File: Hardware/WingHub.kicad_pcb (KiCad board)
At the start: 2 copper layers, 50.8 x 22.9 mm, 17 parts, among them J1 feather long, J2 feather short, J3 USB_A, SW1 RESET, SW2 DOWNLOADER, U1 CH559T

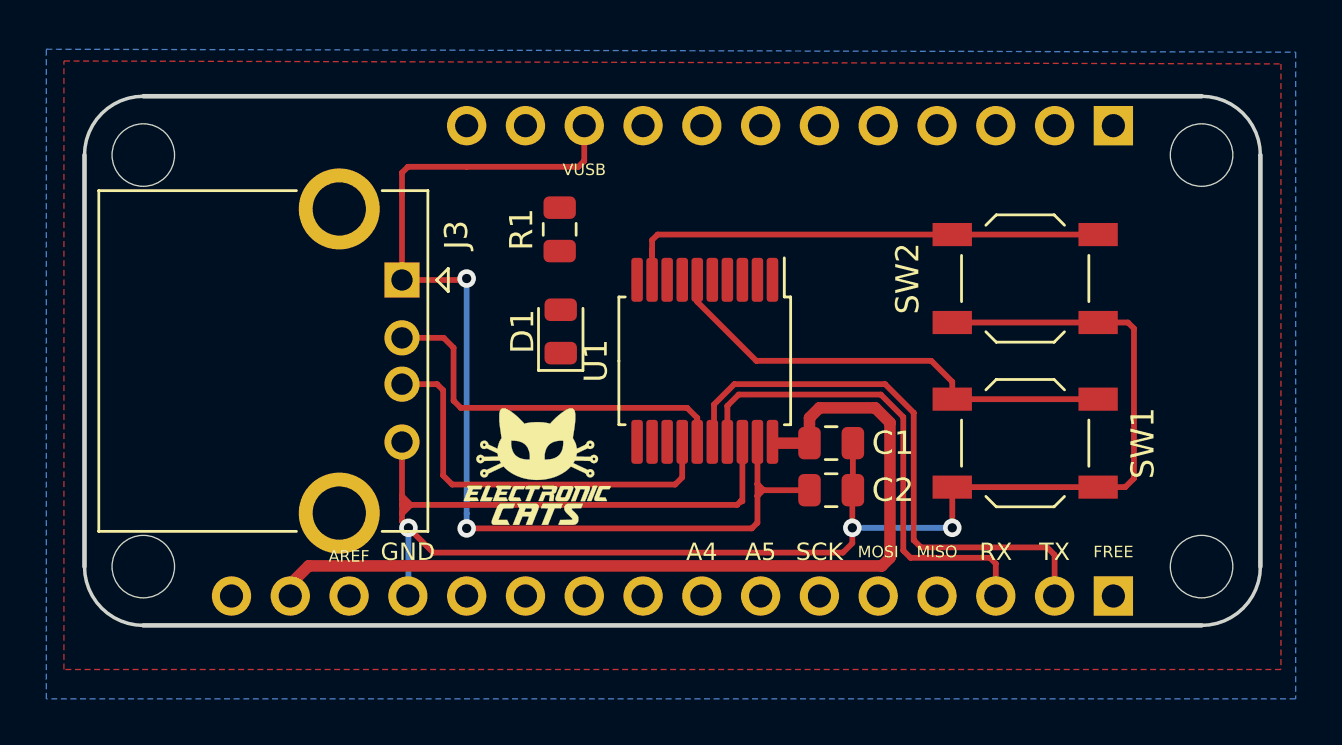
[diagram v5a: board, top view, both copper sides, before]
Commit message: Added electronic devices are routed.
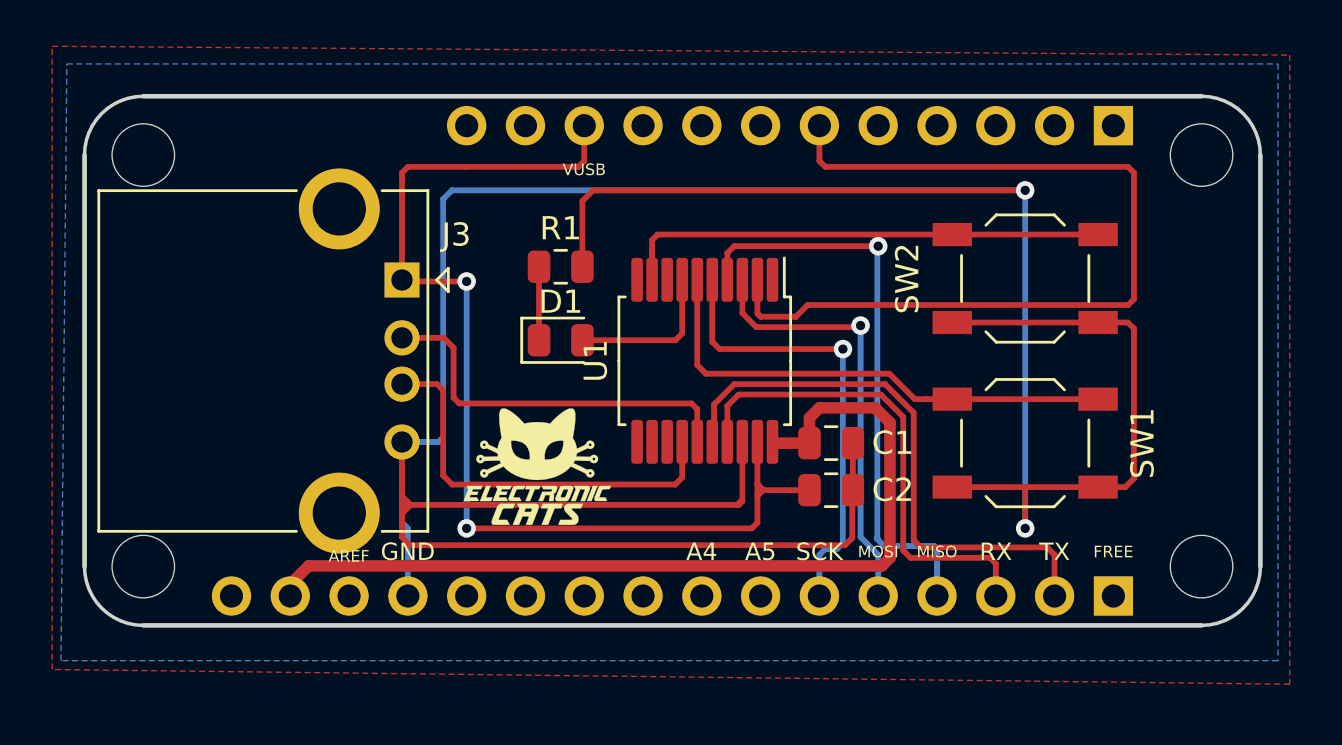
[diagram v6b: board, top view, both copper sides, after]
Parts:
- moved R1 1.62 mm to (46.0, 32.8), turned to 0 degrees
- moved D1 0.38 mm to (46.0, 35.9), turned to 0 degrees
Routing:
- net GND: track 79.2 -> 153.2 mm, vias 3 -> 2
- net /CS: track 0.00 -> 38.9 mm
- net /MISO: track 0.00 -> 25.0 mm, vias 0 -> 1
- net /SCK: track 0.00 -> 19.8 mm, vias 0 -> 1
- net /MOSI: track 0.00 -> 18.8 mm, vias 0 -> 1
- net /LED: track 0.00 -> 6.75 mm
- net Net-(D1-Pad1): track 0.00 -> 3.18 mm
- net /RST: track 20.4 -> 22.6 mm
